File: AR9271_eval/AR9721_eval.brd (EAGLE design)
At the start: 88.1 x 72.7 mm, 125 parts, among them J1 UJ2-MIBH2-4-SMT-TR, J3 HTST-110-01-XX-DV, J7 132134-15, J8 132134-15, U1 U-ATHEROS-AR9271, U2 AT24C04C-XHM-T, U3 LT3080EQPBF, U4 LT3080EQPBF, U5 LT3080EQPBF, U6 LT3080EQPBF, Y1 ECS-400-10-36-CKY-TR

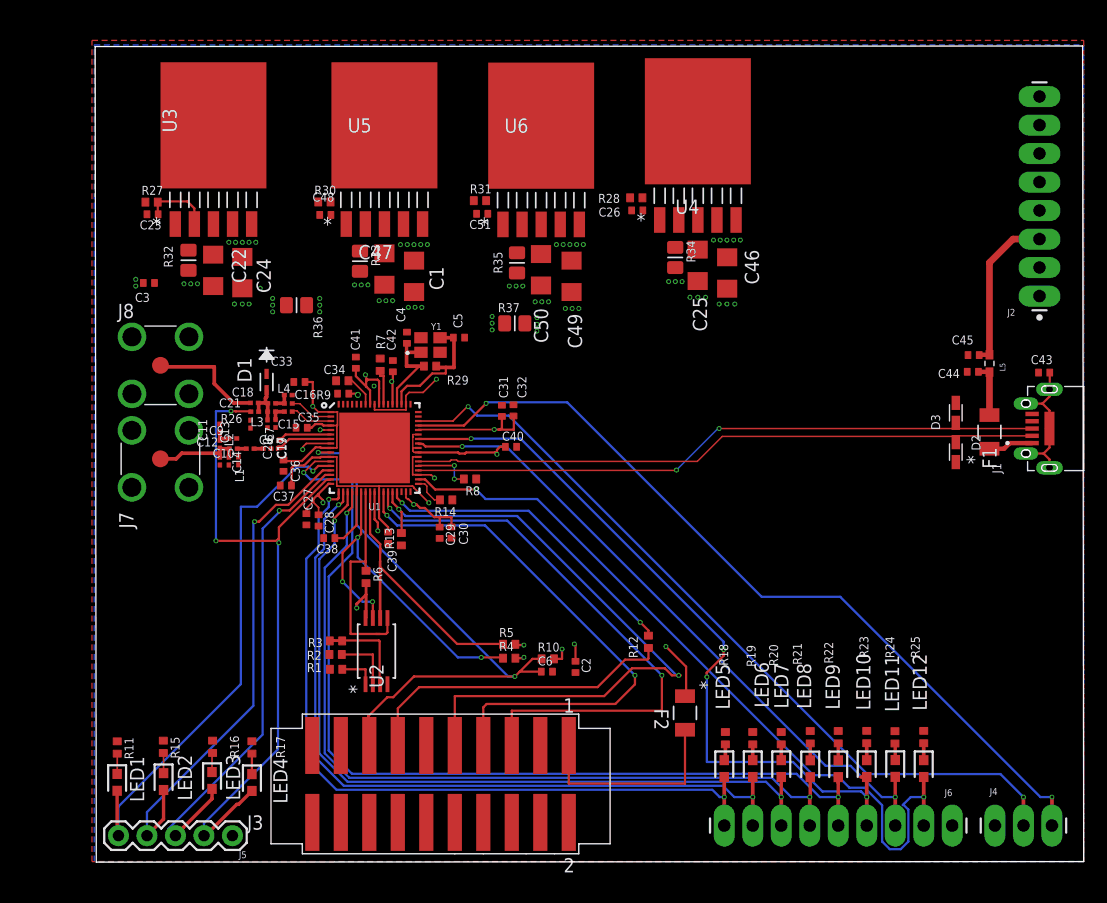
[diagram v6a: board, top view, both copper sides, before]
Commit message: First pass of the updated AR9271 dev board. Took Stephen's fine board, and OCD'd it. Still requires stiching, better LAYER3 power layout, TNAMES cleanup, better stiching, but it's close!
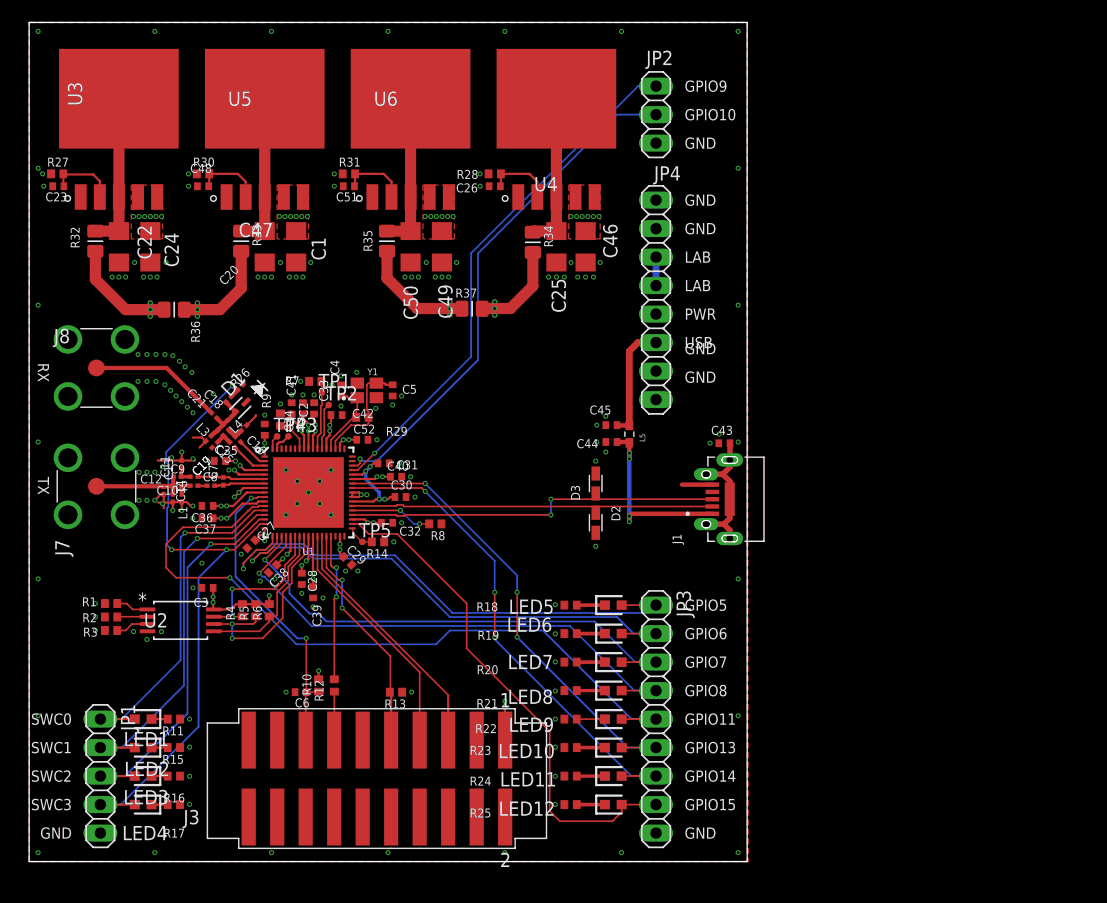
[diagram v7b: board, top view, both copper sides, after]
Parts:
- removed F1, F2: 1206L150THWR, Polyfuse_1206L150:1206LSERIES
- removed J2: (no value), SparkFun-Connectors:1X08_LONGPADS
- removed J4: (no value), SparkFun-Connectors:1X03_LONGPADS
- removed J5: (no value), SparkFun-Connectors:1X05
- removed J6: (no value), SparkFun-Connectors:1X09_LONGPADS
- added C52: 1u, oresat-rcl:.0402-B-NOSILK
- added JP1: (no value), pinhead:1X05
- added JP2: (no value), pinhead:1X03
- added JP3: (no value), pinhead:1X09
- added JP4: (no value), pinhead:1X08
- added TP1, TP2, TP3, TP4, TP5: TPTP06R, testpad:TP06R
- C2: value 100p -> 100n
- C35, C36: value 10.0pF -> 10p
- C37: value 100pF -> 100p
- C38, C40: value 1000pF -> 1n
- C39: value 10nF -> 10n
- C41, C42: value 1uF -> 1u
- R5, R6: value 10k -> 4.7k
- moved C45 32.9 mm to (51.9, 38.9)
- moved C44 32.8 mm to (51.9, 37.4)
- moved C2 32.8 mm to (25.4, 40.4), turned to 90 degrees
- moved D2 32.7 mm to (50.5, 30.2)
- moved D3 32.7 mm to (50.5, 33.7)
- moved L5 32.7 mm to (53.5, 38.1)
- moved R25 32.1 mm to (48.3, 5.08), turned to 0 degrees
- moved C43 29.2 mm to (62.0, 37.3)
- moved J1 29.2 mm to (63.0, 32.3)
- moved R24 29.1 mm to (48.3, 7.62), turned to 0 degrees
- moved R12 28.3 mm to (27.2, 15.7)
- moved LED12 27.9 mm to (52.1, 5.08), turned to 0 degrees
- moved C3 27.7 mm to (15.9, 24.4)
- moved R23 26.4 mm to (48.3, 10.2), turned to 0 degrees
- moved LED11 25.1 mm to (52.1, 7.62), turned to 0 degrees
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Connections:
- net N$11 renamed BIASREF
- net N$16 renamed TDO-PRE-RES
- net N$2 renamed TXRTUNE
- net N$3 renamed EE-WP
- net N$4 renamed EE-SCK
- net N$5 renamed EE-SDA
- net N$8 renamed A1
- net N$9 renamed A2
- net RST_L renamed !RST
- net XTAL_IN renamed XTALI
- net XTAL_OUT renamed XTALO
- removed net N$1: R7.2, U1.58
- removed net N$10: R14.2, U1.35
- removed net N$31: C44.1, F1.2, L5.1
- removed net N$32: F2.2, J3.1
- new net CTRL1: R7.2, TP1.TP, U1.58
- new net CTRL2: TP2.TP, U1.57
- new net PDET: TP4.TP, U1.68
- new net SPIBOOT: R14.2, TP5.TP, U1.35
- new net XPABIOS: TP3.TP, U1.67
- net 1V2_A: now also C2.1
- net 3V3_A: now also C52.1
- net 3V3_D: now also J3.1; no longer C2.1, F2.1
- net GND: now also C52.2, JP1.5, JP2.3, JP3.9, JP4.1, JP4.2, JP4.7, JP4.8; no longer J2.1, J2.2, J2.7, J2.8, J4.1, J5.1, J6.1
- net GPIO10: now also JP2.2; no longer J4.2
- net GPIO11: now also JP3.5; no longer J6.5
- net GPIO13: now also JP3.6; no longer J6.4
- net GPIO14: now also JP3.7; no longer J6.3
- net GPIO15: now also JP3.8; no longer J6.2
- net GPIO5: now also JP3.1; no longer J6.9
- net GPIO6: now also JP3.2; no longer J6.8
- net GPIO7: now also JP3.3; no longer J6.7
- net GPIO8: now also JP3.4; no longer J6.6
- net GPIO9: now also JP2.1; no longer J4.3
- net LDO_IN: now also JP4.5; no longer J2.4
- net N$6: now also JP4.3, JP4.4; no longer J2.5, J2.6
- net SWCOM0: now also JP1.1; no longer J5.5
- net SWCOM1: now also JP1.2; no longer J5.4
- net SWCOM2: now also JP1.3; no longer J5.3
- net SWCOM3: now also JP1.4; no longer J5.2
- net USB+5V: now also JP4.6; no longer J2.3
- net USB_+V: now also C44.1, L5.1; no longer F1.1
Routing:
- net 3V3_D: track 70.7 -> 138.7 mm, vias 19 -> 25
- net LDO_IN: track 12.1 -> 53.3 mm, vias 20 -> 24
- net TCK: track 61.0 -> 20.8 mm
- net TDI: track 51.6 -> 22.8 mm, vias 2 -> 0
- net 1V2_A: track 21.8 -> 50.4 mm, vias 8 -> 9
- net GPIO9: track 74.5 -> 46.7 mm, vias 2 -> 1
- net TMS: track 48.8 -> 21.9 mm, vias 2 -> 0
- net GPIO7: track 71.5 -> 44.9 mm, vias 2 -> 1
- net GPIO8: track 73.5 -> 47.1 mm, vias 2 -> 1
- net GPIO10: track 71.5 -> 46.0 mm, vias 2 -> 1
- net !RST: track 53.0 -> 27.8 mm
- net GPIO15: track 69.7 -> 45.6 mm, vias 2 -> 0
- net TDO: track 28.4 -> 4.33 mm
- net USB_DM: track 56.3 -> 32.8 mm
- net GPIO6: track 69.6 -> 46.2 mm, vias 2 -> 1
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- added copper zone on layer 15, net GND
- added copper zone on layer 1, net LDO_IN
- removed copper zone on layer 15, net 1V2_A
- removed copper zone on layer 15, net 1V2_D
- removed copper zone on layer 15, net 3V3_A
- removed copper zone on layer 15, net 3V3_D
- removed copper zone on layer 15, net LDO_IN
- removed copper zone on layer 1, net RFOUT_N
- removed copper zone on layer 1, net RFOUT_P
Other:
- board size 88.1 x 72.7 mm -> 64 x 74.8 mm
- board text added: "GND"
- board text added: "GPIO10"
- board text added: "GPIO11"
- board text added: "GPIO13"
- board text added: "GPIO14"
- board text added: "GPIO15"
- board text added: "GPIO5"
- board text added: "GPIO6"
- board text added: "GPIO7"
- board text added: "GPIO8"
- board text added: "GPIO9"
- board text added: "LAB"
- board text added: "PWR"
- board text added: "RX"
- board text added: "SWC0"
- board text added: "SWC1"
- board text added: "SWC2"
- board text added: "SWC3"
- board text added: "TX"
- board text added: "USB"
